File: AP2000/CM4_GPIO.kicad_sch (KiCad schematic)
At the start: 26 parts, among them J2 USB_OTG, J3 Boot, J9 0826-1X1T-GH-F, SW1 SW_SPST, U1 CH340N, U2 ATECC608A-MAHDA, U3 SN74LVC07AD, U5 74LVC1G07SE-7

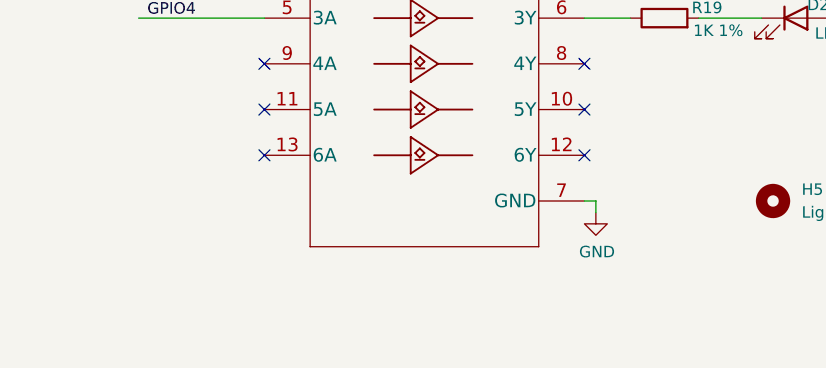
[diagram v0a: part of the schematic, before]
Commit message: Mods to AP2000 for manufacturing. 50 PCBs ordered from JLCPCB with SMd assembly.
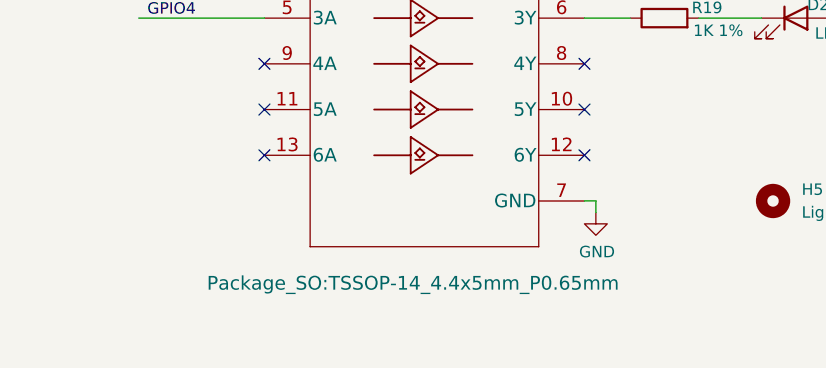
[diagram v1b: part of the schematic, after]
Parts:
- U3: footprint Package_SO:SOIC-14_3.9x8.7mm_P1.27mm -> Package_SO:TSSOP-14_4.4x5mm_P0.65mm; LCSC C7659 -> C7809
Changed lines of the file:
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@@
       (effects (font (size 1.524 1.524)))
     )
-    (property "Footprint" "Package_SO:SOIC-14_3.9x8.7mm_P1.27mm" (id 2) (at 63.5 160.909 0)
-      (effects (font (size 1.524 1.524)) hide)
+    (property "Footprint" "Package_SO:TSSOP-14_4.4x5mm_P0.65mm" (id 2) (at 62.23 186.309 0)
+      (effects (font (size 1.524 1.524)))
     )
     (property "Datasheet" "" (id 3) (at 63.5 159.385 0)
@@
       (effects (font (size 1.27 1.27)) hide)
     )
-    (property "LCSC" "C7659" (id 5) (at 63.5 159.385 0)
+    (property "LCSC" "C7809" (id 5) (at 63.5 159.385 0)
       (effects (font (size 1.27 1.27)) hide)
     )
